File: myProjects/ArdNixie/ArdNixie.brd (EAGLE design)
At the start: 60.6 x 66 mm, 29 parts, among them IC1 74141, IC2 PRO-MINI, IC3 SPARKRTC, IC4 Anode Driver, IC5 74LS595N, P1 s adj, X1 HIV, X2 12V, X3 Hr, X4 Min, X5 Seconds

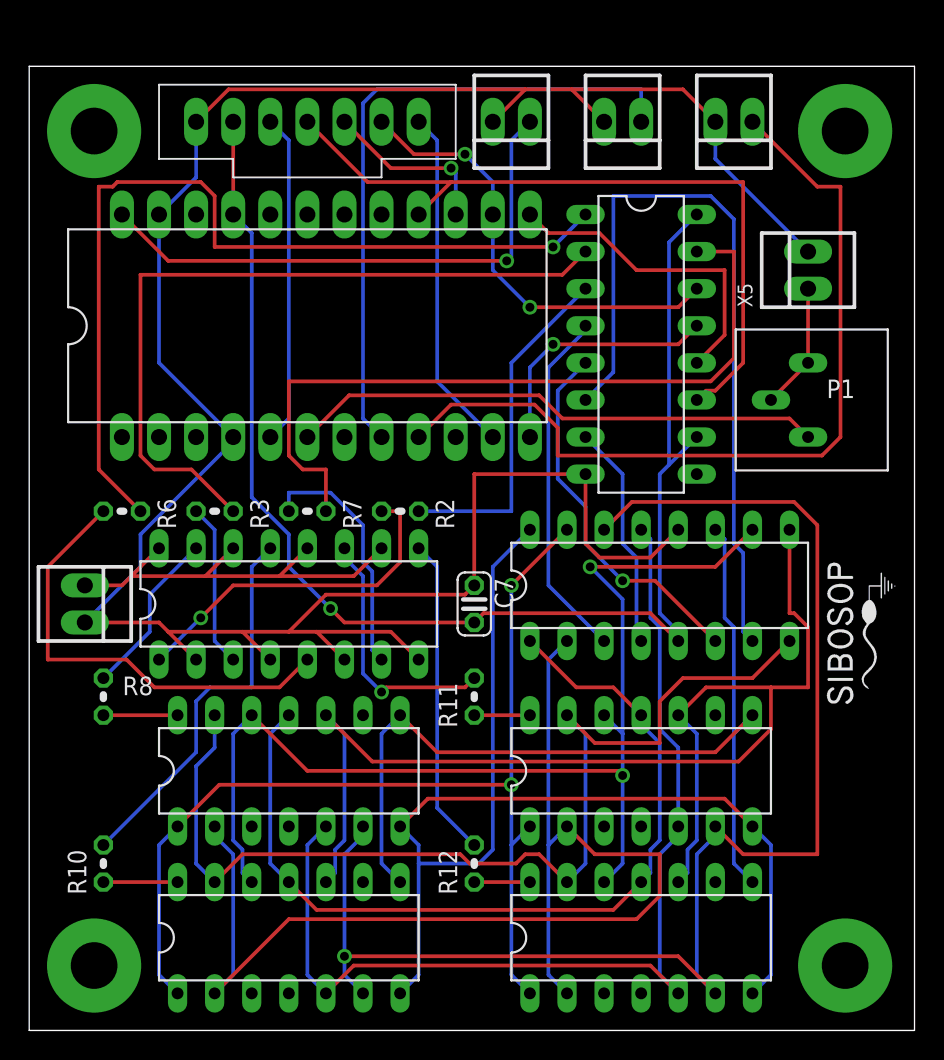
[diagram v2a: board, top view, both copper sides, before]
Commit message: provided some room for nixie headers
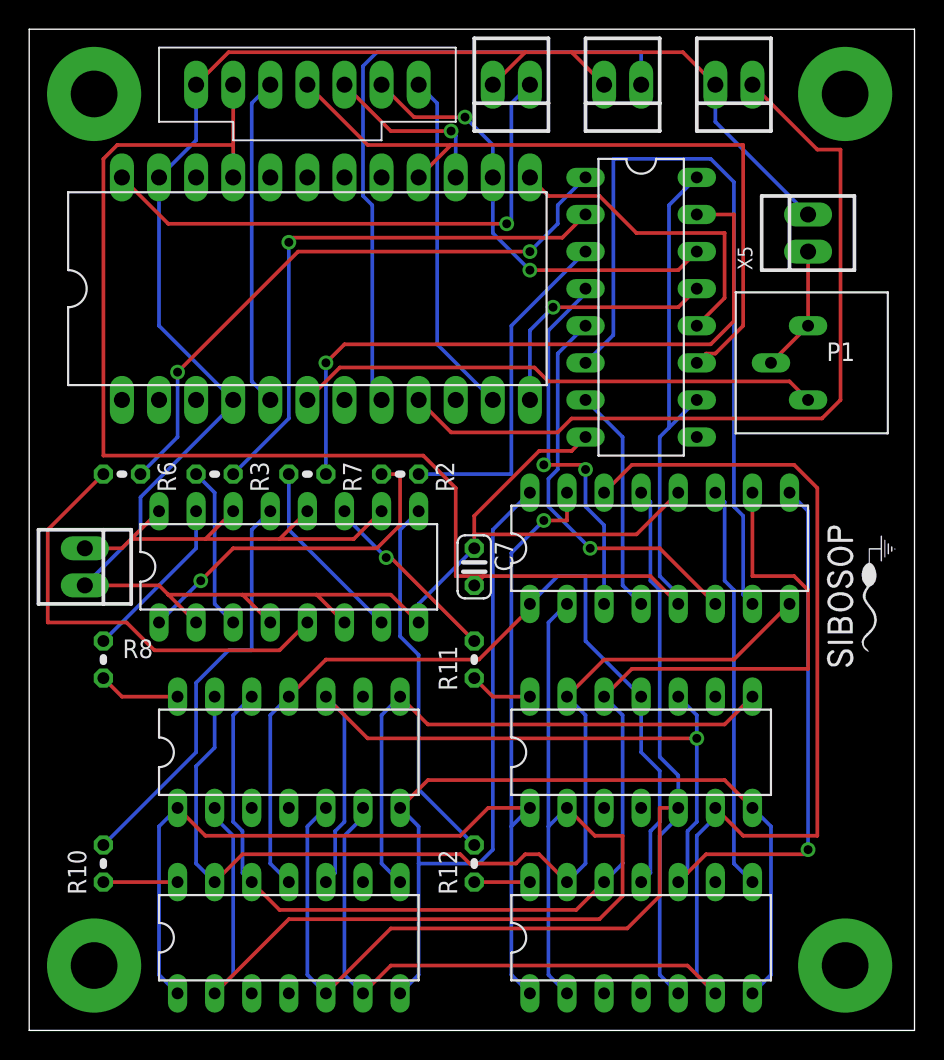
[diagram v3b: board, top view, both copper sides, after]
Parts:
- moved U$5 2.54 mm to (55.9, 64.1)
- moved U$7 2.54 mm to (4.45, 64.1)
- moved IC1 2.54 mm to (43.2, 33.0)
- moved C7 2.54 mm to (30.5, 31.8)
- moved IC2 2.54 mm to (19.1, 50.8)
- moved IC3 2.54 mm to (19.1, 64.8)
- moved IC4 2.54 mm to (17.8, 31.8)
- moved IC5 2.54 mm to (41.9, 49.5)
- moved P1 2.54 mm to (53.3, 45.7)
- moved R11 2.54 mm to (30.5, 25.4)
- moved R2 2.54 mm to (25.4, 38.1)
- moved R3 2.54 mm to (12.7, 38.1)
- moved R6 2.54 mm to (6.35, 38.1)
- moved R7 2.54 mm to (19.1, 38.1)
- moved R8 2.54 mm to (5.08, 25.4)
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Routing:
- net VDD: track 94.8 -> 117.4 mm, vias 1 -> 0
- net N$2: track 61.7 -> 42.2 mm, vias 1 -> 2
- net N$3: track 51.4 -> 38.6 mm, vias 0 -> 1
- net N$11: track 72.0 -> 83.1 mm
- net VSS: track 170.4 -> 162.7 mm
- net N$10: track 81.7 -> 88.9 mm, vias 0 -> 2
- net N$14: track 76.6 -> 83.3 mm, vias 2 -> 0
- net N$8: track 72.2 -> 78.6 mm, vias 2 -> 1
- net N$1: track 51.9 -> 46.6 mm, vias 0 -> 1
- net N$7: track 79.1 -> 84.2 mm
- net N$37: track 17.6 -> 12.8 mm
- net N$26: track 17.0 -> 12.8 mm
- net N$38: track 21.9 -> 25.5 mm
- net N$13: track 65.7 -> 69.0 mm
- net N$21: track 97.8 -> 100.9 mm, vias 1 -> 0
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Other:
- board size 60.6 x 66 mm -> 60.6 x 68.6 mm
